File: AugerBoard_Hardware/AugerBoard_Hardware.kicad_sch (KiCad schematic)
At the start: 44 parts, among them J1 RJ45_LED_Shielded, J2 Conn_01x04_MountingPin, Q1 BSS138, Q2 BSS138, Q3 BSS138, SW1 SW_SPDT, SW2 SW_Push, SW3 SW_Push, SW4 SW_Push, U1 Teensy4.1_DEV-16771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

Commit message: Footprint hai
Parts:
- C1, C6, C7: footprint (none) -> Capacitor_SMD:C_0603_1608Metric_Pad1.08x0.95mm_HandSolder
- Conn1, Conn12, Conn14, Conn8: footprint (none) -> MRDT_Connectors:Square_Anderson_2_H_Side_By_Side_PV
- Conn10, Conn11, Conn4, Conn5: footprint (none) -> MRDT_Connectors:MOLEX_SL_02_Horizontal
- Conn13, Conn15, Conn9: footprint (none) -> MRDT_Connectors:MOLEX_SL_05_Horizontal
- Conn2, Conn3: footprint (none) -> MRDT_Connectors:MOLEX_SL_04_Horizontal
- Conn7: footprint (none) -> MRDT_Connectors:MOLEX_SL_03_Horizontal
- D1, D2, D3, D4, D5, D6: footprint (none) -> LED_SMD:LED_0603_1608Metric_Pad1.05x0.95mm_HandSolder
- J1: footprint (none) -> MRDT_Connectors:RJ45_Teensy
- J2: footprint (none) -> Connector_PinHeader_2.54mm:PinHeader_1x04_P2.54mm_Horizontal
- R1, R2, R3, R4, R5, R6: footprint (none) -> Resistor_SMD:R_0603_1608Metric_Pad0.98x0.95mm_HandSolder
- SW1: footprint (none) -> MRDT_Switches:1P2T_Angled_Slide_GPI-152-3013
- SW2, SW3, SW4: footprint (none) -> Button_Switch_SMD:SW_SPST_TL3305A
- U1: footprint MODULE_DEV-16771 -> MRDT_Shields:Teensy_4_1_Ethernet
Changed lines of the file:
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@@
 			)
 		)
-		(property "Footprint" ""
+		(property "Footprint" "Button_Switch_SMD:SW_SPST_TL3305A"
 			(at 111.76 88.9 0)
 			(effects
@@
 			)
 		)
-		(property "Footprint" ""
+		(property "Footprint" "Button_Switch_SMD:SW_SPST_TL3305A"
 			(at 111.76 116.84 0)
 			(effects
@@
 			)
 		)
-		(property "Footprint" ""
+		(property "Footprint" "MRDT_Connectors:RJ45_Teensy"
 			(at 163.195 100.33 90)
 			(effects
@@
 			)
 		)
-		(property "Footprint" ""
+		(property "Footprint" "MRDT_Connectors:Square_Anderson_2_H_Side_By_Side_PV"
 			(at 293.37 120.65 0)
 			(effects
@@
 			)
 		)
-		(property "Footprint" ""
+		(property "Footprint" "Button_Switch_SMD:SW_SPST_TL3305A"
 			(at 111.76 102.87 0)
 			(effects
@@
 			)
 		)
-		(property "Footprint" ""
+		(property "Footprint" "MRDT_Connectors:MOLEX_SL_04_Horizontal"
 			(at 167.64 36.83 0)
 			(effects
@@
 			)
 		)
-		(property "Footprint" ""
+		(property "Footprint" "LED_SMD:LED_0603_1608Metric_Pad1.05x0.95mm_HandSolder"
 			(at 297.18 46.99 0)
 			(effects
@@
 			)
 		)
-		(property "Footprint" ""
+		(property "Footprint" "LED_SMD:LED_0603_1608Metric_Pad1.05x0.95mm_HandSolder"
 			(at 311.15 46.99 0)
 			(effects
@@
 			)
 		)
-		(property "Footprint" ""
+		(property "Footprint" "MRDT_Connectors:Square_Anderson_2_H_Side_By_Side_PV"
 			(at 293.37 106.68 0)
 			(effects
@@
 			)
 		)
-		(property "Footprint" ""
+		(property "Footprint" "LED_SMD:LED_0603_1608Metric_Pad1.05x0.95mm_HandSolder"
 			(at 323.85 46.99 0)
 			(effects
@@
 			)
 		)
-		(property "Footprint" ""
+		(property "Footprint" "MRDT_Connectors:MOLEX_SL_02_Horizontal"
 			(at 67.31 132.08 0)
 			(effects
@@
 			)
 		)
-		(property "Footprint" ""
+		(property "Footprint" "MRDT_Connectors:Square_Anderson_2_H_Side_By_Side_PV"
 			(at 293.37 171.45 0)
 			(effects
@@
 			)
 		)
-		(property "Footprint" ""
+		(property "Footprint" "MRDT_Connectors:Square_Anderson_2_H_Side_By_Side_PV"
 			(at 15.24 68.58 0)
 			(effects
@@
 			)
 		)
-		(property "Footprint" ""
+		(property "Footprint" "MRDT_Connectors:MOLEX_SL_03_Horizontal"
 			(at 231.14 167.64 0)
 			(effects
@@
 			)
 		)
-		(property "Footprint" ""
+		(property "Footprint" "LED_SMD:LED_0603_1608Metric_Pad1.05x0.95mm_HandSolder"
 			(at 351.79 91.44 0)
 			(effects
@@
 			)
 		)
-		(property "Footprint" ""
+		(property "Footprint" "MRDT_Connectors:MOLEX_SL_04_Horizontal"
 			(at 167.64 59.69 0)
 			(effects
@@
 			)
 		)
-		(property "Footprint" ""
+		(property "Footprint" "Resistor_SMD:R_0603_1608Metric_Pad0.98x0.95mm_HandSolder"
 			(at 350.012 213.36 90)
 			(effects
@@
 			)
 		)
-		(property "Footprint" ""
+		(property "Footprint" "Resistor_SMD:R_0603_1608Metric_Pad0.98x0.95mm_HandSolder"
 			(at 350.012 101.6 90)
 			(effects
@@
 			)
 		)
-		(property "Footprint" ""
+		(property "Footprint" "MRDT_Connectors:Square_Anderson_2_H_Side_By_Side_PV"
 			(at 293.37 152.4 0)
 			(effects
@@
 			)
 		)
-		(property "Footprint" "MODULE_DEV-16771"
+		(property "Footprint" "MRDT_Shields:Teensy_4_1_Ethernet"
 			(at 298.45 85.09 0)
 			(effects
@@
 			)
 		)
-		(property "Footprint" ""
+		(property "Footprint" "LED_SMD:LED_0603_1608Metric_Pad1.05x0.95mm_HandSolder"
 			(at 351.79 203.2 0)
 			(effects
@@
 			)
 		)
-		(property "Footprint" ""
+		(property "Footprint" "MRDT_Connectors:MOLEX_SL_02_Horizontal"
 			(at 67.31 104.14 0)
 			(effects
@@
 			)
 		)
-		(property "Footprint" ""
+		(property "Footprint" "Resistor_SMD:R_0603_1608Metric_Pad0.98x0.95mm_HandSolder"
 			(at 295.402 36.83 90)
 			(effects
@@
 			)
 		)
-		(property "Footprint" ""
+		(property "Footprint" "Connector_PinHeader_2.54mm:PinHeader_1x04_P2.54mm_Horizontal"
 			(at 180.34 160.02 0)
 			(effects
@@
 			)
 		)
-		(property "Footprint" ""
+		(property "Footprint" "Resistor_SMD:R_0603_1608Metric_Pad0.98x0.95mm_HandSolder"
 			(at 350.012 158.75 90)
 			(effects
@@
 			)
 		)
-		(property "Footprint" ""
+		(property "Footprint" "MRDT_Connectors:Square_Anderson_2_H_Side_By_Side_PV"
 			(at 293.37 138.43 0)
 			(effects
@@
 			)
 		)
-		(property "Footprint" ""
+		(property "Footprint" "MRDT_Connectors:MOLEX_SL_05_Horizontal"
 			(at 387.35 118.11 0)
 			(effects
@@
 			)
 		)
-		(property "Footprint" ""
+		(property "Footprint" "MRDT_Connectors:Square_Anderson_2_H_Side_By_Side_PV"
 			(at 293.37 185.42 0)
 			(effects
@@
 			)
 		)
-		(property "Footprint" ""
+		(property "Footprint" "MRDT_Connectors:MOLEX_SL_02_Horizontal"
 			(at 67.31 193.04 0)
 			(effects
@@
 			)
 		)
-		(property "Footprint" ""
+		(property "Footprint" "MRDT_Connectors:Square_Anderson_2_H_Side_By_Side_PV"
 			(at 15.24 55.88 0)
 			(effects
@@
 			)
 		)
-		(property "Footprint" ""
+		(property "Footprint" "Resistor_SMD:R_0603_1608Metric_Pad0.98x0.95mm_HandSolder"
 			(at 322.072 36.83 90)
 			(effects
@@
 			)
 		)
-		(property "Footprint" ""
+		(property "Footprint" "MRDT_Connectors:MOLEX_SL_05_Horizontal"
 			(at 386.08 229.87 0)
 			(effects
@@
 			)
 		)
-		(property "Footprint" ""
+		(property "Footprint" "MRDT_Connectors:MOLEX_SL_05_Horizontal"
 			(at 387.35 175.26 0)
 			(effects
@@
 			)
 		)
-		(property "Footprint" ""
+		(property "Footprint" "Resistor_SMD:R_0603_1608Metric_Pad0.98x0.95mm_HandSolder"
 			(at 309.372 36.83 90)
 			(effects
@@
 			)
 		)
-		(property "Footprint" ""
+		(property "Footprint" "Capacitor_SMD:C_0603_1608Metric_Pad1.08x0.95mm_HandSolder"
 			(at 88.5952 52.07 0)
 			(effects
@@
 			)
 		)
-		(property "Footprint" ""
+		(property "Footprint" "Capacitor_SMD:C_0603_1608Metric_Pad1.08x0.95mm_HandSolder"
 			(at 149.86 119.6848 0)
 			(effects
@@
 			)
 		)
-		(property "Footprint" ""
+		(property "Footprint" "MRDT_Switches:1P2T_Angled_Slide_GPI-152-3013"
 			(at 121.92 170.18 0)
 			(effects
@@
 			)
 		)
-		(property "Footprint" ""
+		(property "Footprint" "Capacitor_SMD:C_0603_1608Metric_Pad1.08x0.95mm_HandSolder"
 			(at 119.0752 52.07 0)
 			(effects
@@
 			)
 		)
-		(property "Footprint" ""
+		(property "Footprint" "MRDT_Connectors:MOLEX_SL_02_Horizontal"
 			(at 67.31 162.56 0)
 			(effects
@@
 			)
 		)
-		(property "Footprint" ""
+		(property "Footprint" "LED_SMD:LED_0603_1608Metric_Pad1.05x0.95mm_HandSolder"
 			(at 351.79 148.59 0)
 			(effects

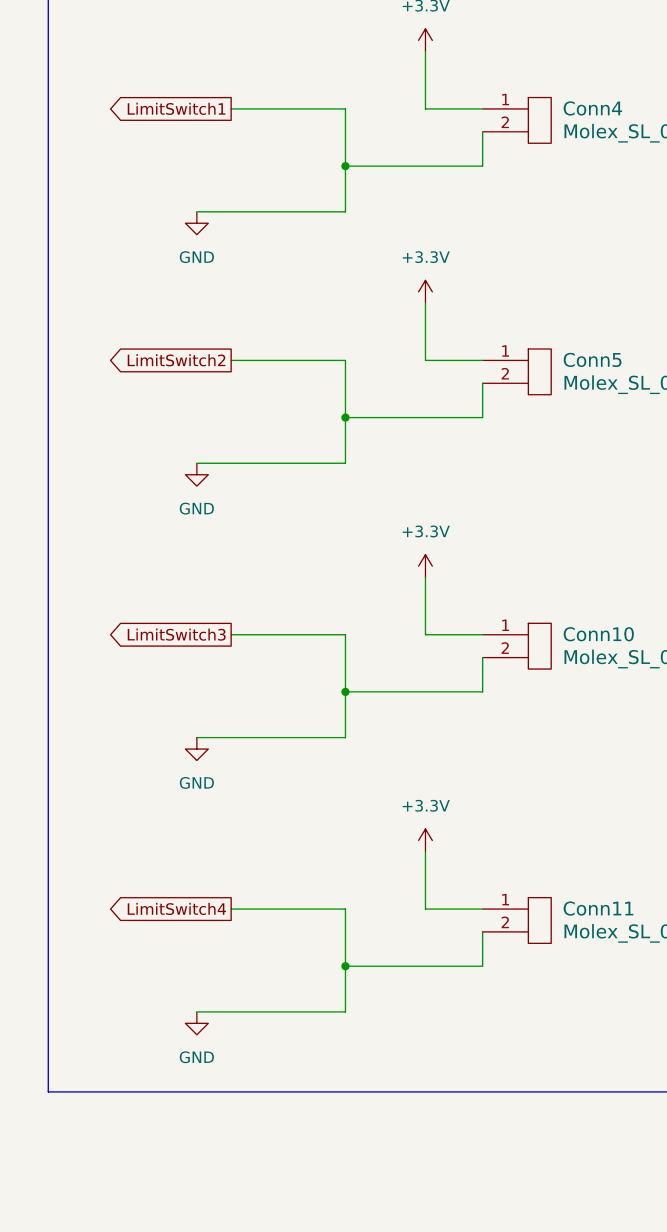
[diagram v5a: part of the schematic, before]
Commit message: Footprint changed and layout started
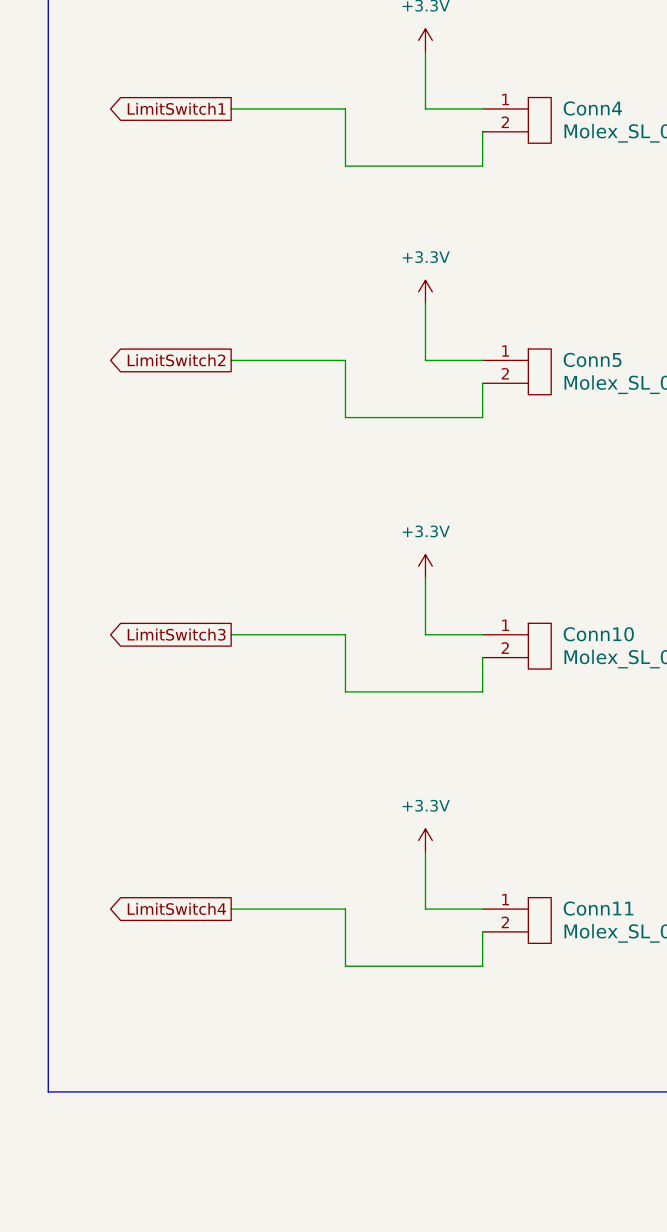
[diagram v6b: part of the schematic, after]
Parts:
- SW1: footprint MRDT_Switches:1P2T_Angled_Slide_GPI-152-3013 -> Button_Switch_THT:SW_Slide_SPDT_Straight_CK_OS102011MS2Q
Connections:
- net GND: no longer Conn10.2, Conn11.2, Conn4.2, Conn5.2, U1.0 (RX1), U1.1 (TX1), U1.7 (RX2), U1.8 (TX2)
- new net LimitSwitch1: Conn4.2, U1.0 (RX1)
- new net LimitSwitch2: Conn5.2, U1.1 (TX1)
- new net LimitSwitch3: Conn10.2, U1.7 (RX2)
- new net LimitSwitch4: Conn11.2, U1.8 (TX2)
